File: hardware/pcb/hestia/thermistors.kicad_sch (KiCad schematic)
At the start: 56 parts

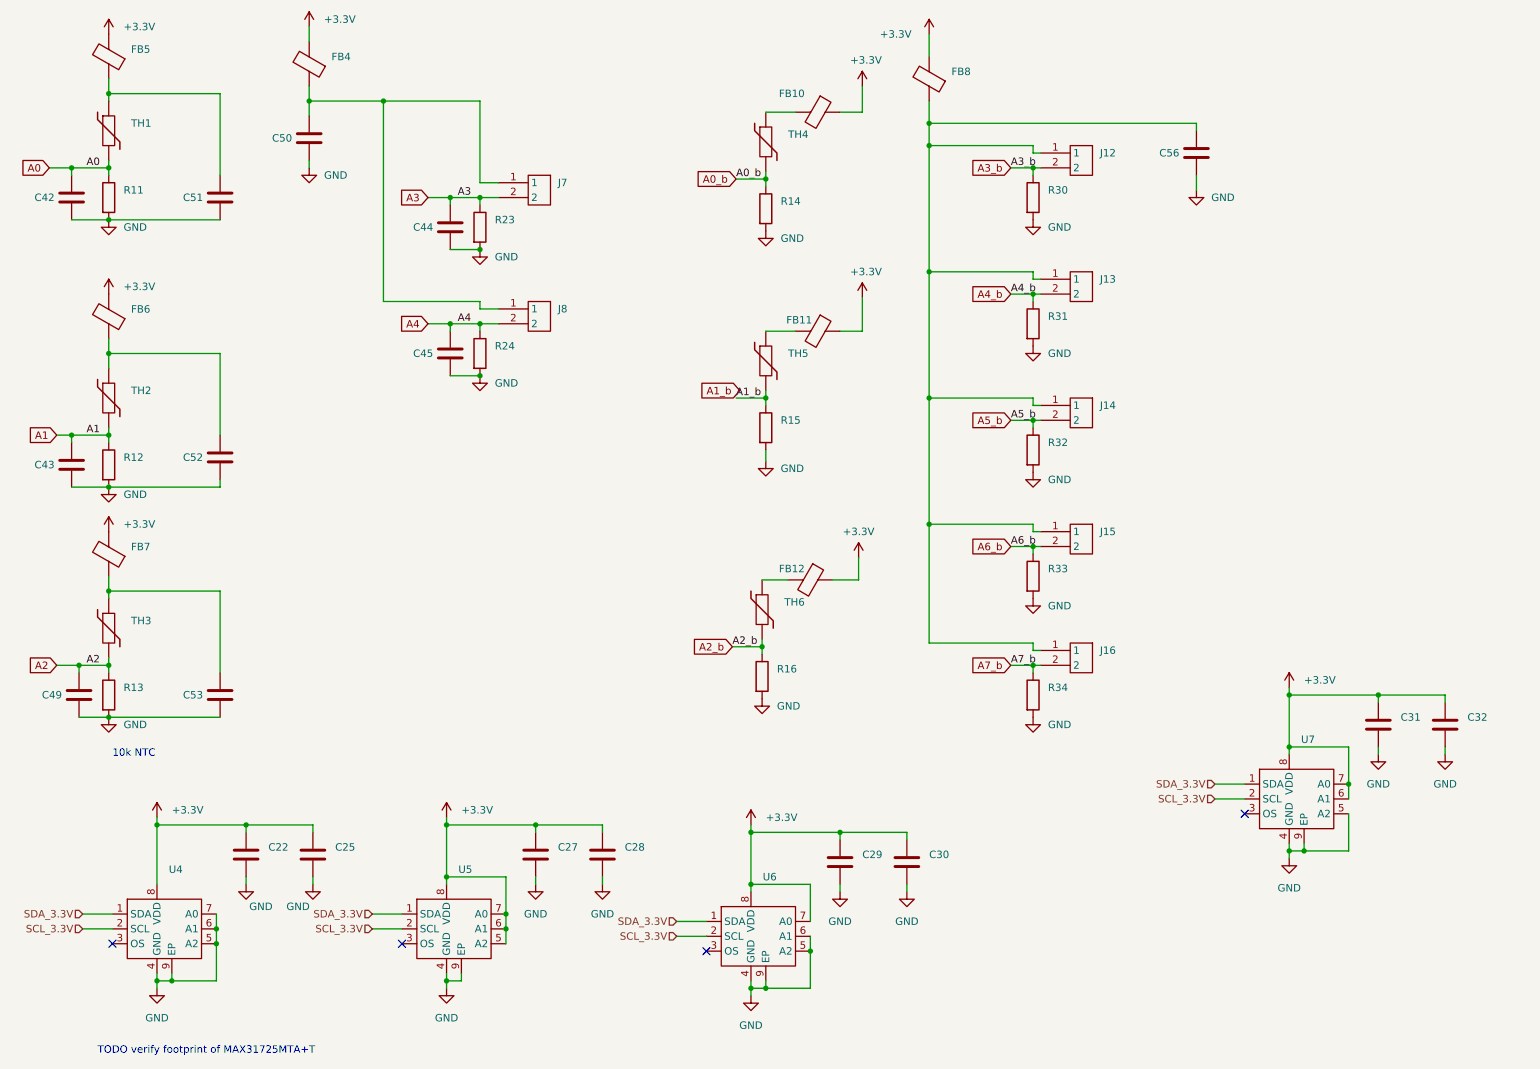
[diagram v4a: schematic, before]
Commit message: added more digikey part numbers to schematic
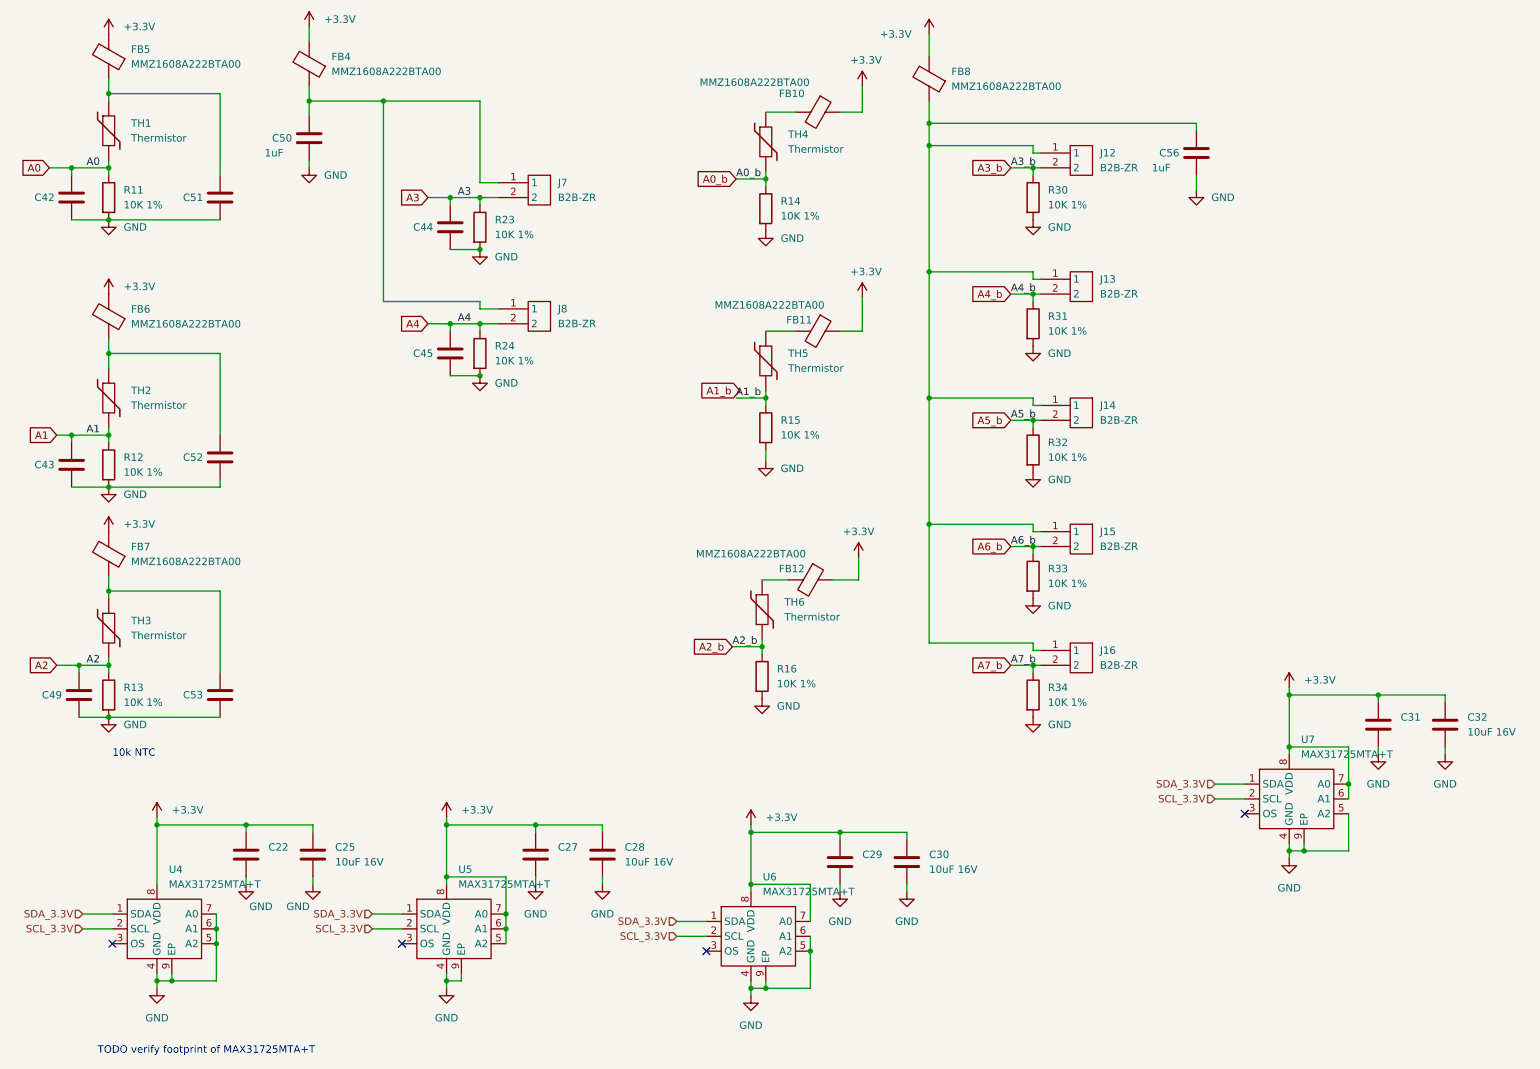
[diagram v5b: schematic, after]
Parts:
- C22, C27, C29, C31, C42, C43, C44, C45, C49, C51, C52, C53: Digikey Part (none) -> 1276-CL10B104KB8WPNDCT-ND
- C25, C28, C30, C32: value (none) -> 10uF 16V; footprint (none) -> Capacitor_SMD:C_0603_1608Metric_Pad1.08x0.95mm_HandSolder
- C50, C56: value (none) -> 1uF; footprint (none) -> Capacitor_SMD:C_0603_1608Metric_Pad1.08x0.95mm_HandSolder
- FB10, FB11, FB12, FB4, FB5, FB6, FB7, FB8: value (none) -> MMZ1608A222BTA00; footprint (none) -> Resistor_SMD:R_0603_1608Metric_Pad0.98x0.95mm_HandSolder
- J12, J13, J14, J15, J16, J7, J8: value (none) -> B2B-ZR; footprint (none) -> Hestia:B2B-ZR(LF)(SN)
- R11, R12, R13, R14, R15, R16, R23, R24, R30, R31, R32, R33, R34: value (none) -> 10K 1%; footprint (none) -> Resistor_SMD:R_0603_1608Metric_Pad0.98x0.95mm_HandSolder
- TH1, TH2, TH3, TH4, TH5, TH6: value (none) -> Thermistor; footprint (none) -> Resistor_SMD:R_0603_1608Metric_Pad0.98x0.95mm_HandSolder
- U4, U5, U6, U7: value (none) -> MAX31725MTA+T; footprint (none) -> Package_DFN_QFN:DFN-8-1EP_3x3mm_P0.65mm_EP1.55x2.4mm

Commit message: added more digikey part numbers to schematic
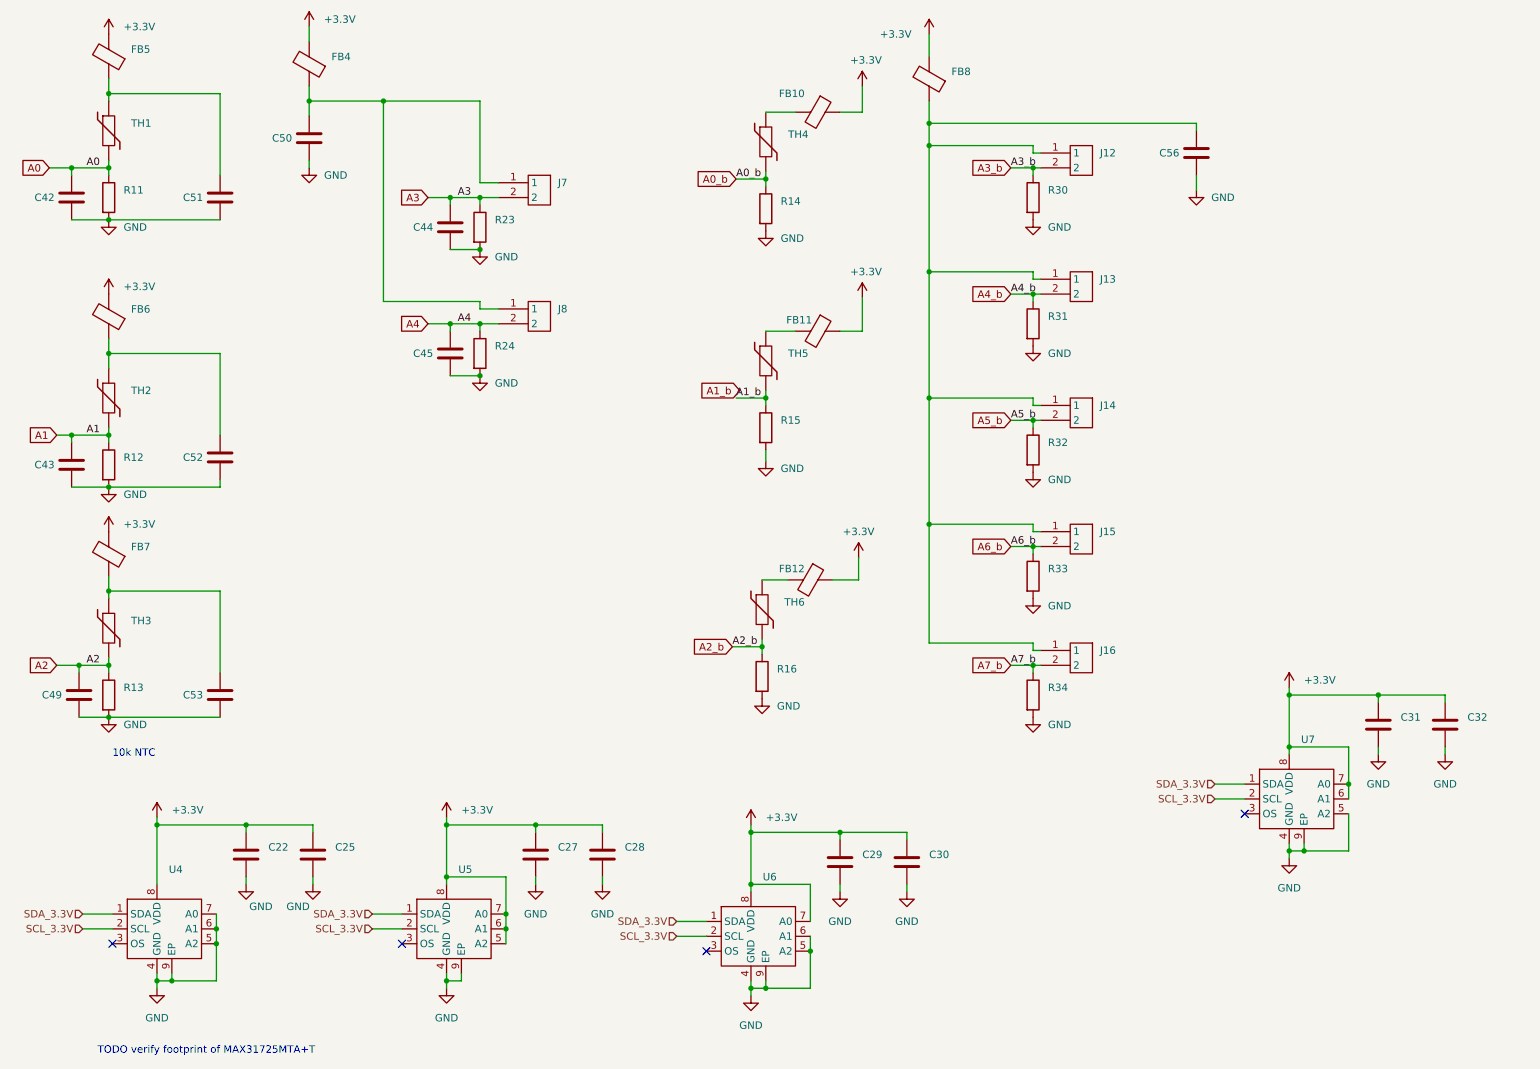
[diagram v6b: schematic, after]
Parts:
- C25, C28, C30, C32: value 10uF 16V -> (none); footprint Capacitor_SMD:C_0603_1608Metric_Pad1.08x0.95mm_HandSolder -> (none); Digikey Part (none) -> 311-1822-1-ND
- C50, C56: value 1uF -> (none); footprint Capacitor_SMD:C_0603_1608Metric_Pad1.08x0.95mm_HandSolder -> (none); Digikey Part (none) -> 478-12231-1-ND
- FB10, FB11, FB12, FB4, FB5, FB6, FB7, FB8: value MMZ1608A222BTA00 -> (none); footprint Resistor_SMD:R_0603_1608Metric_Pad0.98x0.95mm_HandSolder -> (none)
- J12, J13, J14, J15, J16, J7, J8: value B2B-ZR -> (none); footprint Hestia:B2B-ZR(LF)(SN) -> (none)
- R11, R12, R13, R14, R15, R16, R23, R24, R30, R31, R32, R33, R34: value 10K 1% -> (none); footprint Resistor_SMD:R_0603_1608Metric_Pad0.98x0.95mm_HandSolder -> (none)
- TH1, TH2, TH3, TH4, TH5, TH6: value Thermistor -> (none); footprint Resistor_SMD:R_0603_1608Metric_Pad0.98x0.95mm_HandSolder -> (none)
- U4, U5, U6, U7: value MAX31725MTA+T -> (none); footprint Package_DFN_QFN:DFN-8-1EP_3x3mm_P0.65mm_EP1.55x2.4mm -> (none)

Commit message: Fix some ERC violations
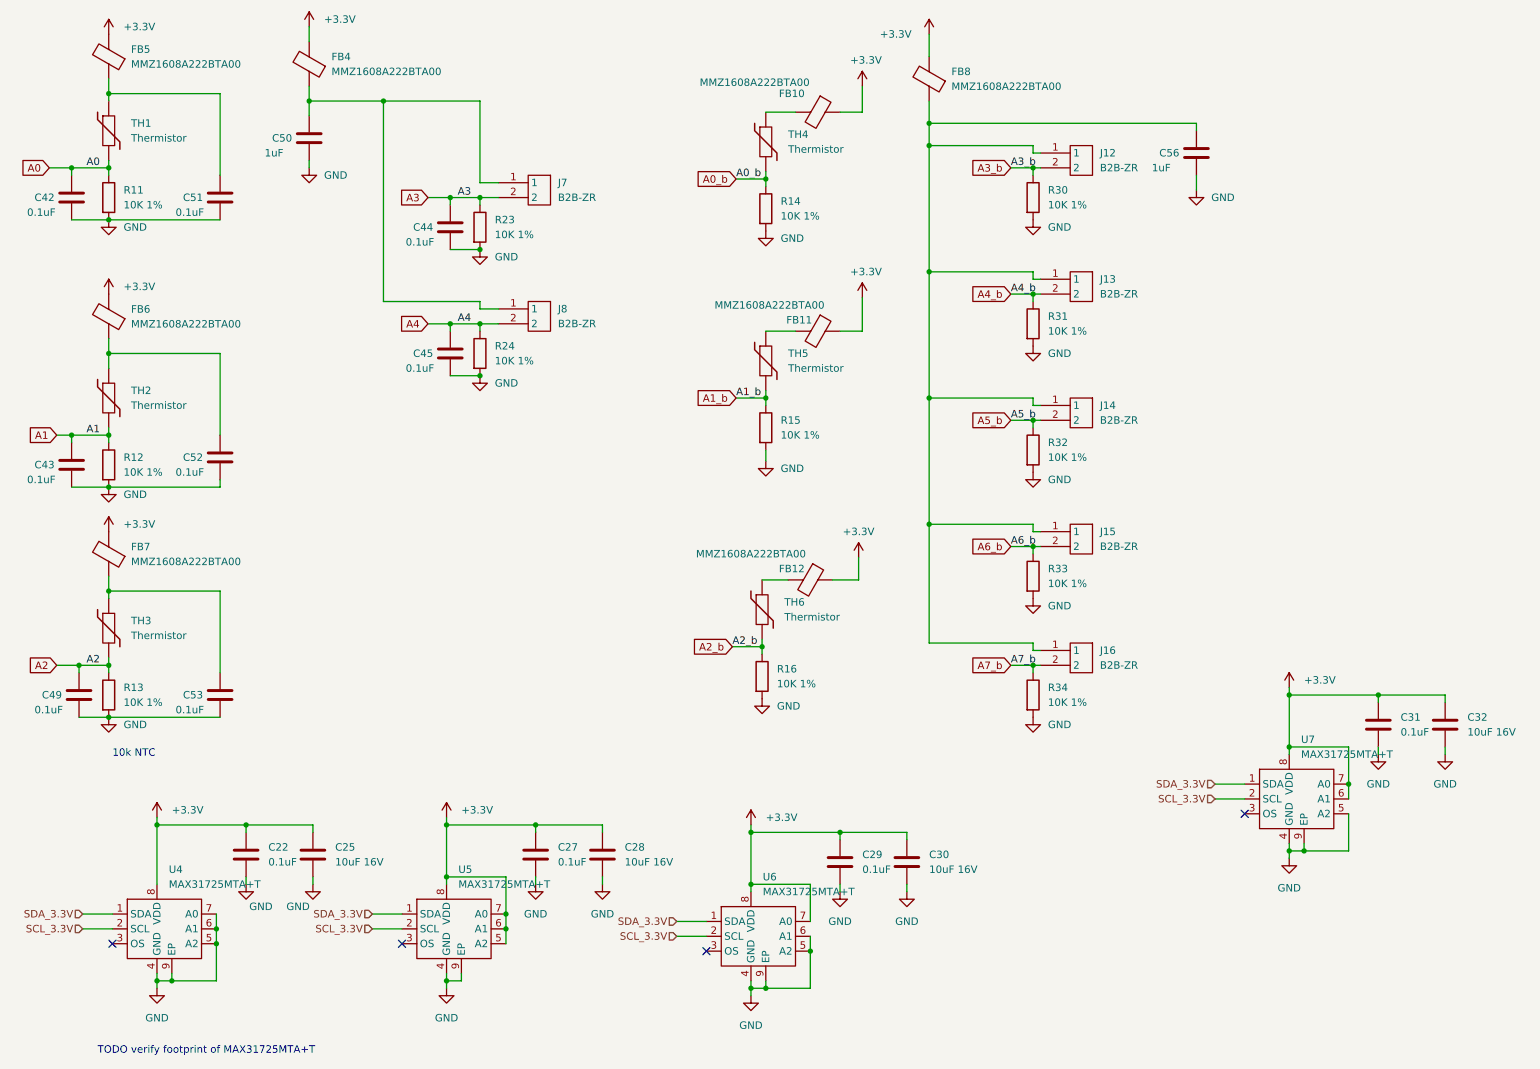
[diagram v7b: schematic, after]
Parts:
- C22, C27, C29, C31, C42, C43, C44, C45, C49, C51, C52, C53: value (none) -> 0.1uF; footprint (none) -> Capacitor_SMD:C_0603_1608Metric_Pad1.08x0.95mm_HandSolder
- C25, C28, C30, C32: value (none) -> 10uF 16V; footprint (none) -> Capacitor_SMD:C_0603_1608Metric_Pad1.08x0.95mm_HandSolder
- C50, C56: value (none) -> 1uF; footprint (none) -> Capacitor_SMD:C_0603_1608Metric_Pad1.08x0.95mm_HandSolder
- FB10, FB11, FB12, FB4, FB5, FB6, FB7, FB8: value (none) -> MMZ1608A222BTA00; footprint (none) -> Resistor_SMD:R_0603_1608Metric_Pad0.98x0.95mm_HandSolder
- J12, J13, J14, J15, J16, J7, J8: value (none) -> B2B-ZR; footprint (none) -> Hestia:B2B-ZR(LF)(SN)
- R11, R12, R13, R14, R15, R16, R23, R24, R30, R31, R32, R33, R34: value (none) -> 10K 1%; footprint (none) -> Resistor_SMD:R_0603_1608Metric_Pad0.98x0.95mm_HandSolder
- TH1, TH2, TH3, TH4, TH5, TH6: value (none) -> Thermistor; footprint (none) -> Resistor_SMD:R_0603_1608Metric_Pad0.98x0.95mm_HandSolder
- U4, U5, U6, U7: value (none) -> MAX31725MTA+T; footprint (none) -> Package_DFN_QFN:DFN-8-1EP_3x3mm_P0.65mm_EP1.55x2.4mm
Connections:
- net +3V3 renamed +3.3V

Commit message: changed all 10K to 0.5% to be same component. changed led part numbers back to 0805. - my mistake. i had thought the footprints had changed to 0603. filled in other missing digikey part numbers. added manufacturer names and manufacturer part numbers. finished adding SMD/TH entry for component types. Excluded R4/R5 DNP part numbers from BOM
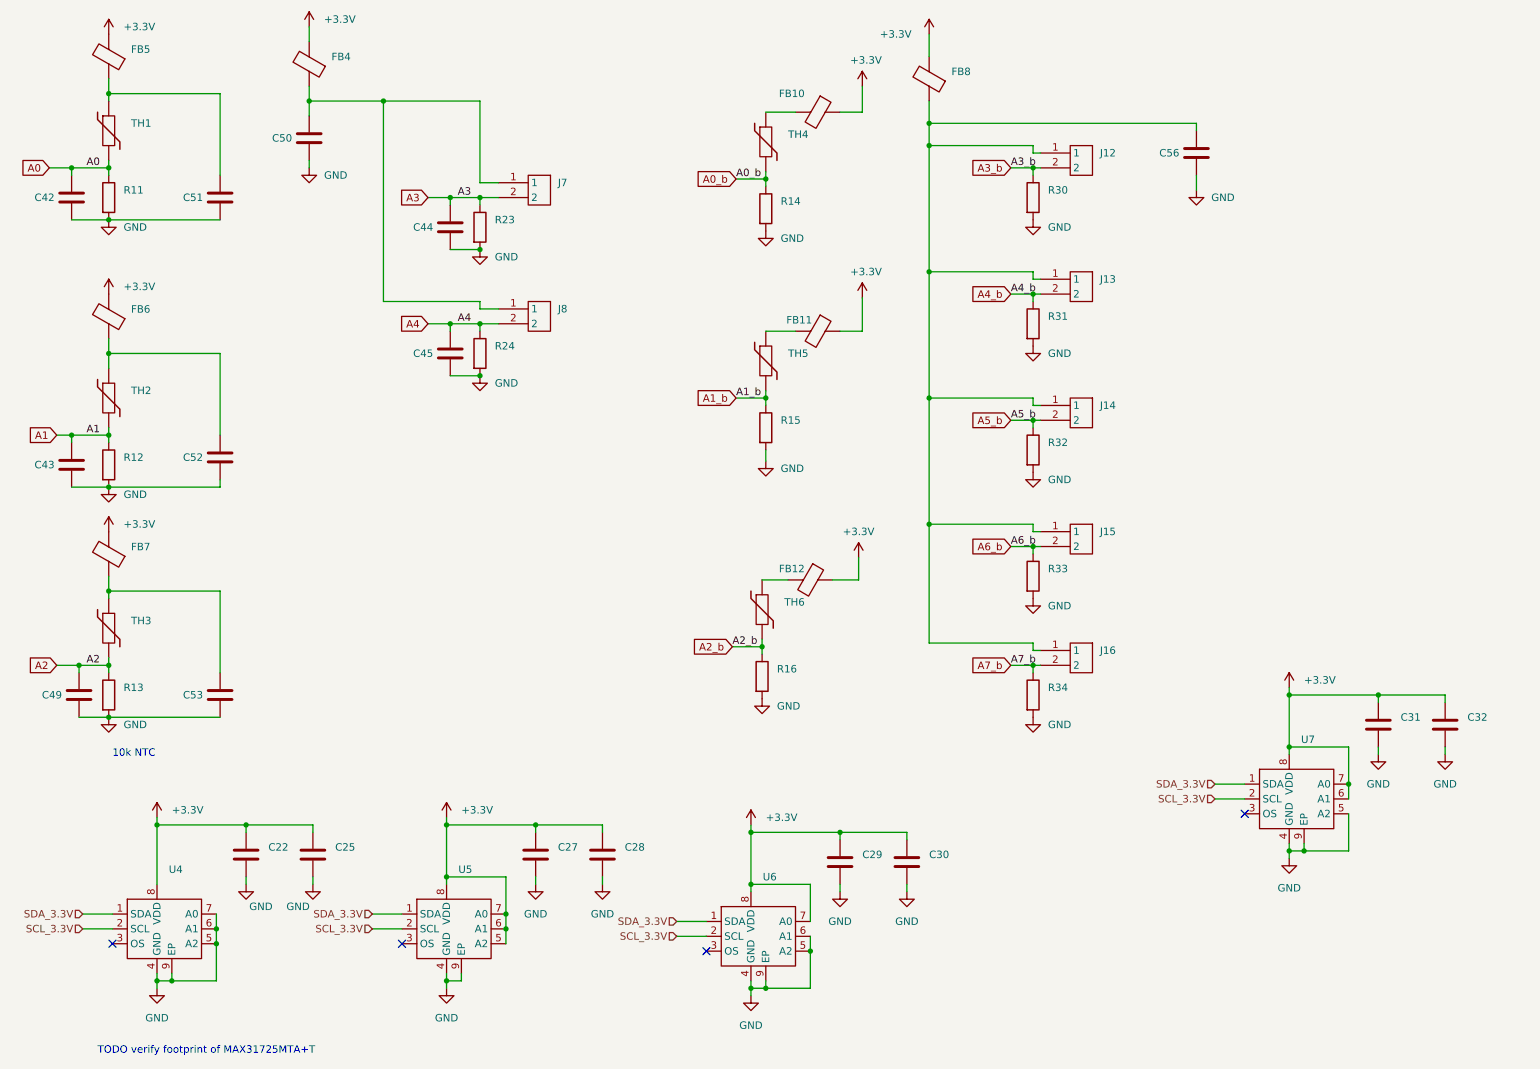
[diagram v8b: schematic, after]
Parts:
- C22, C27, C29, C31, C42, C43, C44, C45, C49, C51, C52, C53: value 0.1uF -> (none); footprint Capacitor_SMD:C_0603_1608Metric_Pad1.08x0.95mm_HandSolder -> (none); Manufacturer (none) -> Samsung Electro-Mechanics; Mfr PN (none) -> CL10B104KB8WPND
- C25, C28, C30, C32: value 10uF 16V -> (none); footprint Capacitor_SMD:C_0603_1608Metric_Pad1.08x0.95mm_HandSolder -> (none); Manufacturer (none) -> YAGEO; Mfr PN (none) -> CC0603MRX5R7BB106
- C50, C56: value 1uF -> (none); footprint Capacitor_SMD:C_0603_1608Metric_Pad1.08x0.95mm_HandSolder -> (none); Manufacturer (none) -> KYOCERA AVX; Mfr PN (none) -> 0603ZC105MAT2A
- FB10, FB11, FB12, FB4, FB5, FB6, FB7, FB8: value MMZ1608A222BTA00 -> (none); footprint Resistor_SMD:R_0603_1608Metric_Pad0.98x0.95mm_HandSolder -> (none); Manufacturer (none) -> TDK; Mfr PN (none) -> MMZ1608A222BTA00
- J12, J13, J14, J15, J16, J7, J8: value B2B-ZR -> (none); footprint Hestia:B2B-ZR(LF)(SN) -> (none); Digikey Part (none) -> 455-1657-ND; Manufacturer (none) -> JST Sales America Inc.; Mfr PN (none) -> B2B-ZR(LF)(SN); Type (none) -> TH
- R11, R12, R13, R14, R15, R16, R23, R24, R30, R31, R32, R33, R34: value 10K 1% -> (none); footprint Resistor_SMD:R_0603_1608Metric_Pad0.98x0.95mm_HandSolder -> (none); Digikey Part (none) -> RR08P10.0KDCT-ND; Manufacturer (none) -> Susumu; Mfr PN (none) -> RR0816P-103-D
- TH1, TH2, TH3, TH4, TH5, TH6: value Thermistor -> (none); footprint Resistor_SMD:R_0603_1608Metric_Pad0.98x0.95mm_HandSolder -> (none); Digikey Part (none) -> 478-12936-1-ND; Manufacturer (none) -> KYOCERA AVX; Mfr PN (none) -> NB21K00103JBB
- U4, U5, U6, U7: value MAX31725MTA+T -> (none); footprint Package_DFN_QFN:DFN-8-1EP_3x3mm_P0.65mm_EP1.55x2.4mm -> (none); Manufacturer Maxim -> Analog Devices Inc./Maxim Integrated; Mfr PN (none) -> MAX31725MTA+T
